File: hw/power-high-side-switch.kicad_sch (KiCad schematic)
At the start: 2 parts, among them Q1701 DMN3032LFDBQ-13

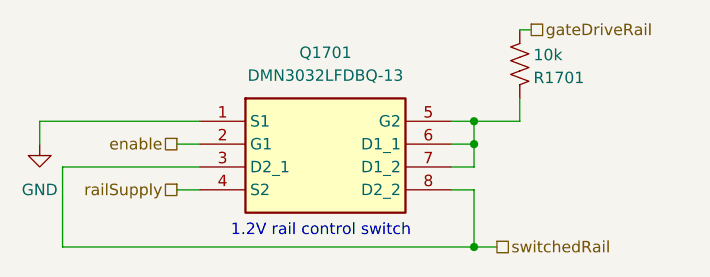
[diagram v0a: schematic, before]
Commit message: Tx LPF and its selection is pretty much done. Fix some OCD. Start to describe the design and construction.
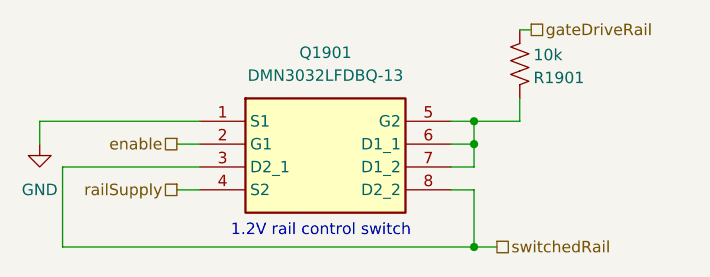
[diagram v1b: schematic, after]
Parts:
- renumbered Q1701 to Q1901, R1701 to R1901
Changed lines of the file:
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@@
 		(dnp no)
 		(fields_autoplaced yes)
-		(property "Reference" "Q1701"
+		(property "Reference" "Q1901"
 			(at 156.21 139.7 0)
 			(effects
@@
 				)
 				(path "/8ae46c04-d01a-4756-8774-512b694bfaff/cbf7569b-90aa-4e1a-84a7-d4153f6242b6/87586e12-4e8a-4bfb-a4d8-78ecafab6fec"
-					(reference "Q1701")
+					(reference "Q1901")
 					(unit 1)
 				)
@@
 		(dnp no)
 		(fields_autoplaced yes)
-		(property "Reference" "#PWR01701"
+		(property "Reference" "#PWR01901"
 			(at 124.46 156.21 0)
 			(effects
@@
 			(project "USB-SSB-txcvr"
 				(path "/8ae46c04-d01a-4756-8774-512b694bfaff/cbf7569b-90aa-4e1a-84a7-d4153f6242b6/87586e12-4e8a-4bfb-a4d8-78ecafab6fec"
-					(reference "#PWR01701")
+					(reference "#PWR01901")
 					(unit 1)
 				)
@@
 		(on_board yes)
 		(dnp no)
-		(property "Reference" "R1701"
+		(property "Reference" "R1901"
 			(at 179.324 142.494 0)
 			(effects
@@
 			(project "USB-SSB-txcvr"
 				(path "/8ae46c04-d01a-4756-8774-512b694bfaff/cbf7569b-90aa-4e1a-84a7-d4153f6242b6/87586e12-4e8a-4bfb-a4d8-78ecafab6fec"
-					(reference "R1701")
-					(unit 1)
-				)
+					(reference "R1901")
+					(unit 1)
+				)

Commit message: Checkpoint
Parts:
- removed Q1901: DMN3032LFDBQ-13, DMN3032LFDBQ13, symbol DMN3032LFDBQ-13:DMN3032LFDBQ-13
- removed R1901: 10k, symbol Device:R_US
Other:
- note removed: "1.2V rail control switch"
